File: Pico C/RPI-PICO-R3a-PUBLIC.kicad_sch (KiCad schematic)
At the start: 38 parts, among them IC1 W25Q16JVUXIQ, J3 USB_C_Receptacle_USB2.0_16P, J4 SM03B-SRSS-TB, Q1 DMG1012T-7, U2 RT6150B-33GQW, Y1 ECS-120-8-33-JGN-TR

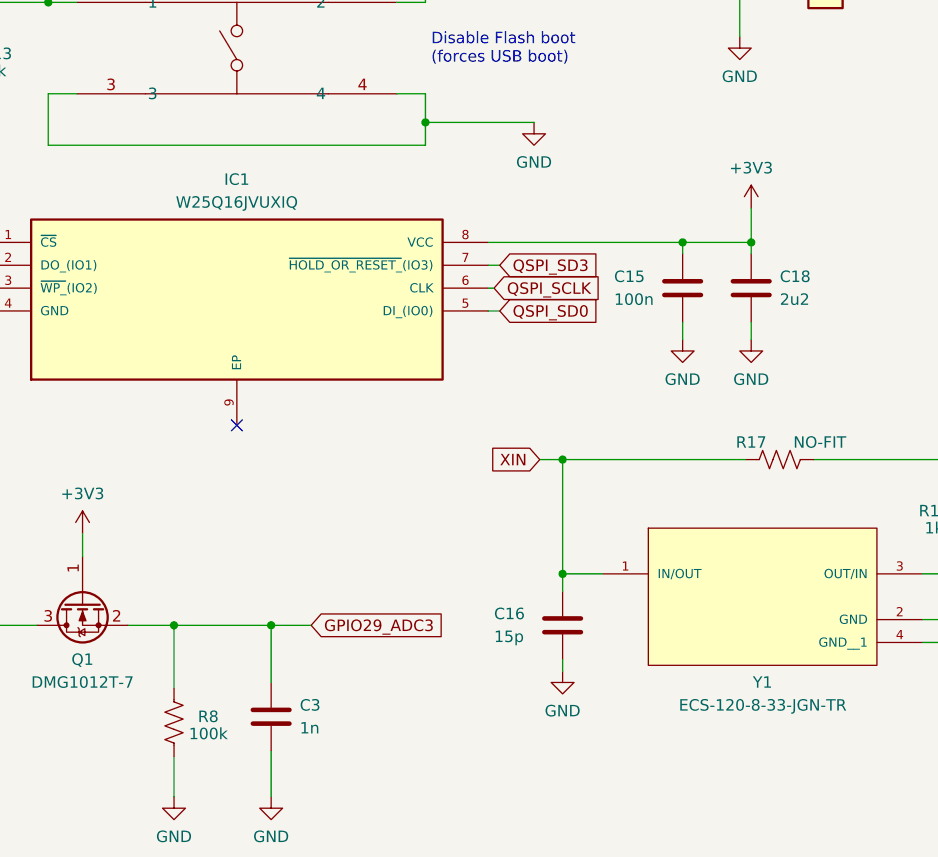
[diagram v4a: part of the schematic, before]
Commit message: Add files via upload
Updated component references to more closely match the original Pico.
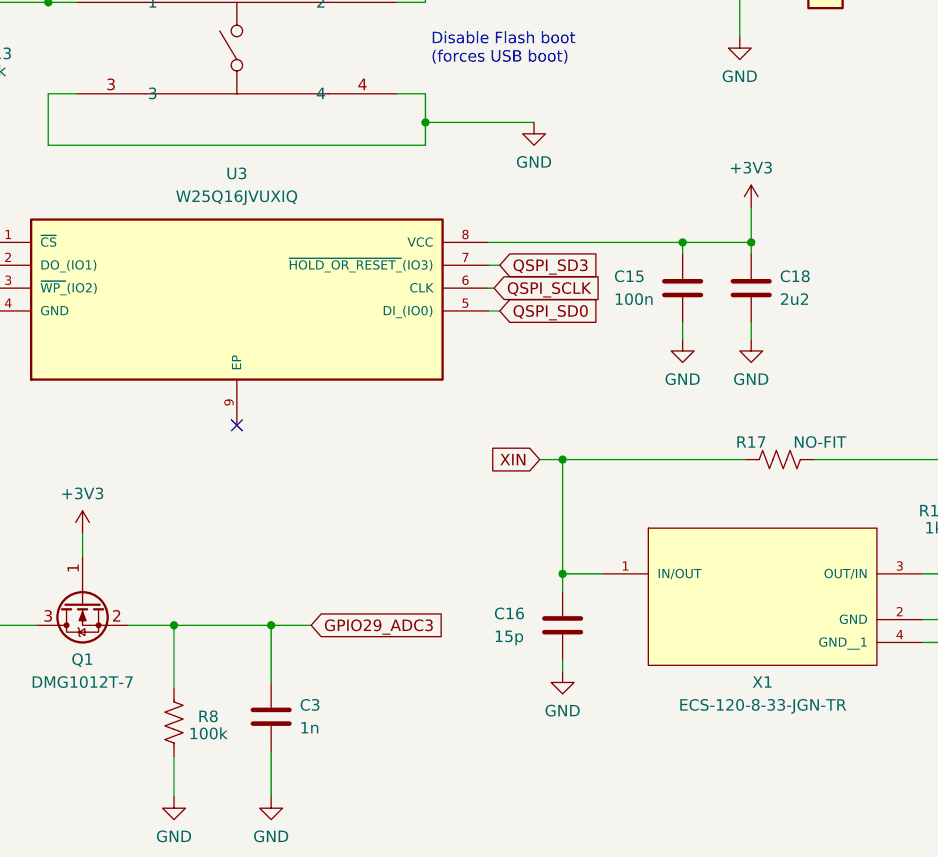
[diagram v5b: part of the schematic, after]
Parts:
- removed IC1: W25Q16JVUXIQ, Pico_C:SON50P300X200X60-9N, symbol Pico_C:W25Q16JVUXIQ
- removed Y1: ECS-120-8-33-JGN-TR, Pico_C:XTAL_ECS-120-8-33-JGN-TR, symbol Pico_C:ECS-120-8-33-JGN-TR
- added U3: W25Q16JVUXIQ, Pico_C:SON50P300X200X60-9N, symbol Pico_C:W25Q16JVUXIQ
- added X1: ECS-120-8-33-JGN-TR, ECS-120-8-33-JGN-TR:XTAL_ECS-120-8-33-JGN-TR, symbol Pico_C:ECS-120-8-33-JGN-TR
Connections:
- net +3V3: now also U3.8 (VCC)
- net GND: now also U3.4 (GND), X1.2 (GND), X1.4 (GND__1)
- net QSPI_SCLK: now also U3.6 (CLK)
- net QSPI_SD0: now also U3.5 (DI_(IO0))
- net QSPI_SD1: now also U3.2 (DO_(IO1))
- net QSPI_SD2: now also U3.3 (~{WP_}(IO2))
- net QSPI_SD3: now also U3.7 (~{HOLD_OR_RESET_}(IO3))
- net QSPI_SS: now also U3.1 (~{CS})
- net XIN: now also X1.1 (IN/OUT)
- net XR: now also X1.3 (OUT/IN)
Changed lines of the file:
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@@
 	)
 	(symbol
-		(lib_id "Pico_C:ECS-120-8-33-JGN-TR")
-		(at 207.645 149.225 0)
-		(unit 1)
-		(exclude_from_sim no)
-		(in_bom yes)
-		(on_board yes)
-		(dnp no)
-		(property "Reference" "Y1"
-			(at 207.645 158.75 0)
-			(effects
-				(font
-					(size 1.27 1.27)
-				)
-			)
-		)
-		(property "Value" "ECS-120-8-33-JGN-TR"
-			(at 207.645 161.29 0)
-			(effects
-				(font
-					(size 1.27 1.27)
-				)
-			)
-		)
-		(property "Footprint" "Pico_C:XTAL_ECS-120-8-33-JGN-TR"
-			(at 207.645 149.225 0)
-			(effects
-				(font
-					(size 1.27 1.27)
-				)
-				(justify bottom)
-				(hide yes)
-			)
-		)
-		(property "Datasheet" "https://ecsxtal.com/store/pdf/ecx-32.pdf"
-			(at 207.645 149.225 0)
-			(effects
-				(font
-					(size 1.27 1.27)
-				)
-				(hide yes)
-			)
-		)
-		(property "Description" ""
-			(at 207.645 149.225 0)
-			(effects
-				(font
-					(size 1.27 1.27)
-				)
-				(hide yes)
-			)
-		)
-		(pin "2"
-		)
-		(pin "3"
-		)
-		(pin "1"
-		)
-		(pin "4"
-		)
-		(instances
-			(project "RPI-PICO-R3a-PUBLIC"
-				(path "/f8a1033e-7d4e-4018-9b4c-1da5b150b31c"
-					(reference "Y1")
-					(unit 1)
-				)
-			)
-		)
-	)
-	(symbol
 		(lib_id "Device:R_US")
 		(at 77.47 50.165 180)
@@
 	)
 	(symbol
+		(lib_id "Pico_C:W25Q16JVUXIQ")
+		(at 121.285 109.855 0)
+		(unit 1)
+		(exclude_from_sim no)
+		(in_bom yes)
+		(on_board yes)
+		(dnp no)
+		(fields_autoplaced yes)
+		(property "Reference" "U3"
+			(at 149.225 102.235 0)
+			(effects
+				(font
+					(size 1.27 1.27)
+				)
+			)
+		)
+		(property "Value" "W25Q16JVUXIQ"
+			(at 149.225 104.775 0)
+			(effects
+				(font
+					(size 1.27 1.27)
+				)
+			)
+		)
+		(property "Footprint" "Pico_C:SON50P300X200X60-9N"
+			(at 121.285 109.855 0)
+			(effects
+				(font
+					(size 1.27 1.27)
+				)
+				(justify bottom)
+				(hide yes)
+			)
+		)
+		(property "Datasheet" "https://www.winbond.com/resource-files/w25q16jv%20spi%20revh%2004082019%20plus.pdf"
+			(at 121.285 109.855 0)
+			(effects
+				(font
+					(size 1.27 1.27)
+				)
+				(hide yes)
+			)
+		)
+		(property "Description" ""
+			(at 121.285 109.855 0)
+			(effects
+				(font
+					(size 1.27 1.27)
+				)
+				(hide yes)
+			)
+		)
+		(pin "9"
+		)
+		(pin "6"
+		)
+		(pin "3"
+		)
+		(pin "4"
+		)
+		(pin "1"
+		)
+		(pin "2"
+		)
+		(pin "5"
+		)
+		(pin "7"
+		)
+		(pin "8"
+		)
+		(instances
+			(project "RPI-PICO-R3a-PUBLIC"
+				(path "/f8a1033e-7d4e-4018-9b4c-1da5b150b31c"
+					(reference "U3")
+					(unit 1)
+				)
+			)
+		)
+	)
+	(symbol
 		(lib_id "Device:R_US")
 		(at 120.65 147.32 180)
@@
 	)
 	(symbol
+		(lib_id "Pico_C:ECS-120-8-33-JGN-TR")
+		(at 207.645 149.225 0)
+		(unit 1)
+		(exclude_from_sim no)
+		(in_bom yes)
+		(on_board yes)
+		(dnp no)
+		(property "Reference" "X1"
+			(at 207.645 158.75 0)
+			(effects
+				(font
+					(size 1.27 1.27)
+				)
+			)
+		)
+		(property "Value" "ECS-120-8-33-JGN-TR"
+			(at 207.645 161.29 0)
+			(effects
+				(font
+					(size 1.27 1.27)
+				)
+			)
+		)
+		(property "Footprint" "ECS-120-8-33-JGN-TR:XTAL_ECS-120-8-33-JGN-TR"
+			(at 207.645 149.225 0)
+			(effects
+				(font
+					(size 1.27 1.27)
+				)
+				(justify bottom)
+				(hide yes)
+			)
+		)
+		(property "Datasheet" "https://ecsxtal.com/store/pdf/ecx-32.pdf"
+			(at 207.645 149.225 0)
+			(effects
+				(font
+					(size 1.27 1.27)
+				)
+				(hide yes)
+			)
+		)
+		(property "Description" ""
+			(at 207.645 149.225 0)
+			(effects
+				(font
+					(size 1.27 1.27)
+				)
+				(hide yes)
+			)
+		)
+		(pin "4"
+		)
+		(pin "2"
+		)
+		(pin "1"
+		)
+		(pin "3"
+		)
+		(instances
+			(project "RPI-PICO-R3a-PUBLIC"
+				(path "/f8a1033e-7d4e-4018-9b4c-1da5b150b31c"
+					(reference "X1")
+					(unit 1)
+				)
+			)
+		)
+	)
+	(symbol
 		(lib_id "Pico_C:SM03B-SRSS-TB_LF__SN_")
 		(at 269.875 135.89 0)
@@
 					(unit 1)
 				)
-			)
-		)
-	)
-	(symbol
-		(lib_id "Pico_C:W25Q16JVUXIQ")
-		(at 121.285 109.855 0)
-		(unit 1)
-		(exclude_from_sim no)
-		(in_bom yes)
-		(on_board yes)
-		(dnp no)
-		(fields_autoplaced yes)
-		(property "Reference" "IC1"
-			(at 149.225 102.87 0)
-			(effects
-				(font
-					(size 1.27 1.27)
-				)
-			)
-		)
-		(property "Value" "W25Q16JVUXIQ"
-			(at 149.225 105.41 0)
-			(effects
-				(font
-					(size 1.27 1.27)
-				)
-			)
-		)
-		(property "Footprint" "Pico_C:SON50P300X200X60-9N"
-			(at 121.285 109.855 0)
-			(effects
-				(font
-					(size 1.27 1.27)
-				)
-				(justify bottom)
-				(hide yes)
-			)
-		)
-		(property "Datasheet" "https://www.winbond.com/resource-files/w25q16jv%20spi%20revh%2004082019%20plus.pdf"
-			(at 121.285 109.855 0)
-			(effects
-				(font
-					(size 1.27 1.27)
-				)
-				(hide yes)
-			)
-		)
-		(property "Description" ""
-			(at 121.285 109.855 0)
-			(effects
-				(font
-					(size 1.27 1.27)
-				)
-				(hide yes)
-			)
-		)
-		(pin "9"
-		)
-		(pin "8"
-		)
-		(pin "4"
-		)
-		(pin "7"
-		)
-		(pin "2"
-		)
-		(pin "6"
-		)
-		(pin "1"
-		)
-		(pin "3"
-		)
-		(pin "5"
-		)
-		(instances
-			(project "RPI-PICO-R3a-PUBLIC"
-				(path "/f8a1033e-7d4e-4018-9b4c-1da5b150b31c"
-					(reference "IC1")
-					(unit 1)
-				)

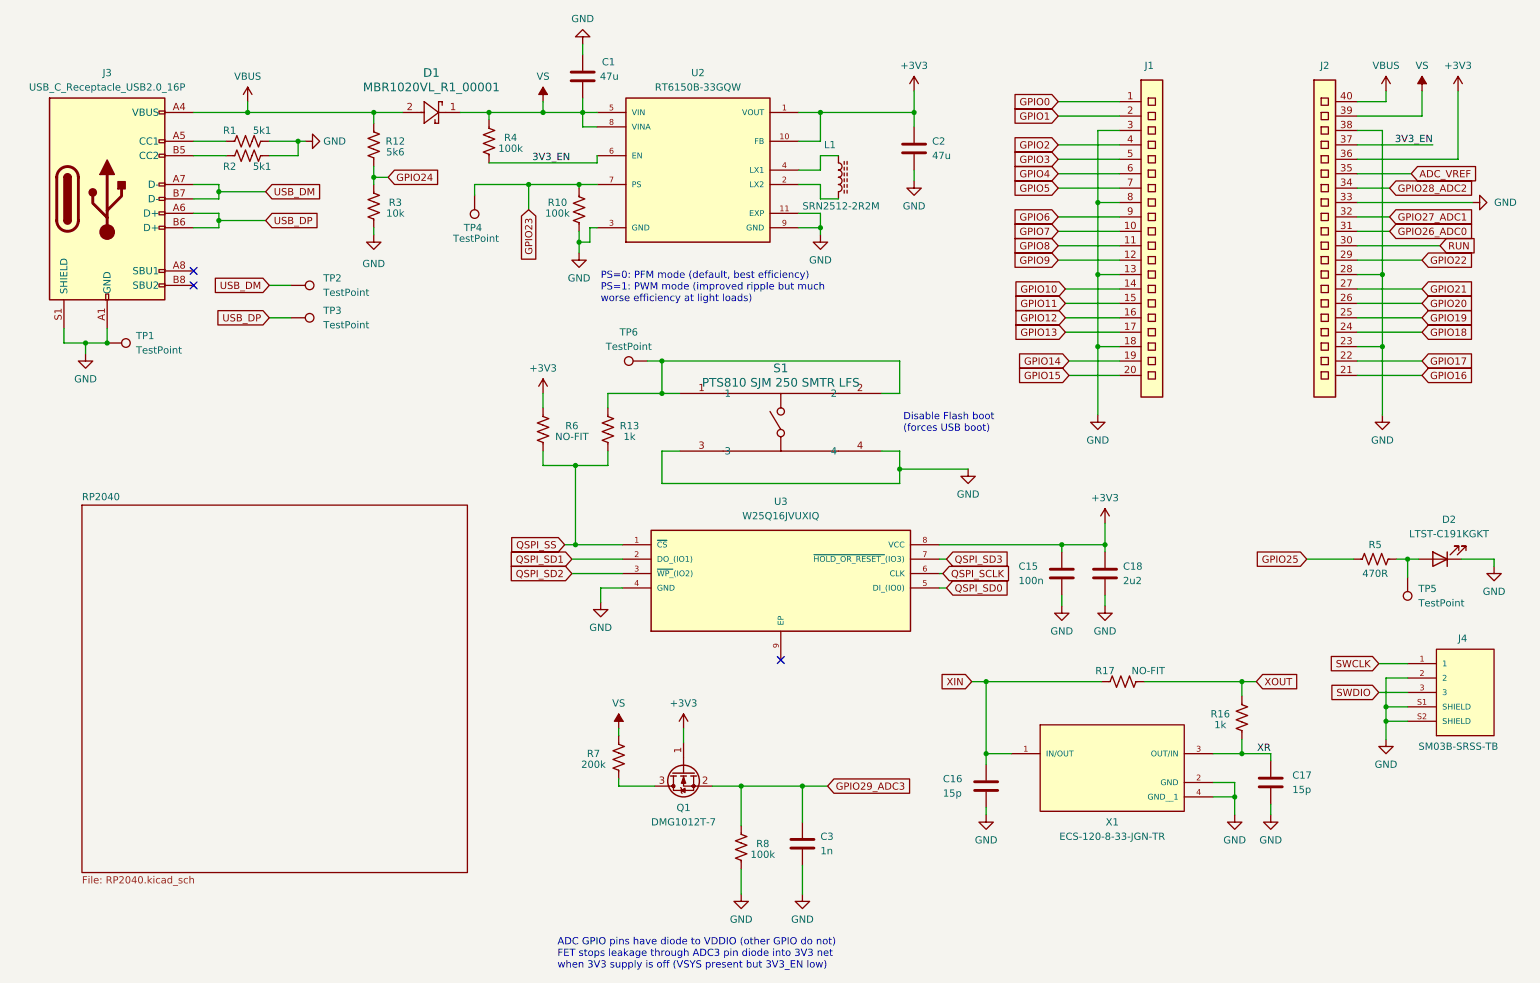
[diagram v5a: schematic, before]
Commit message: Add files via upload
Changed resistor reference numbers to match the real Pico H.
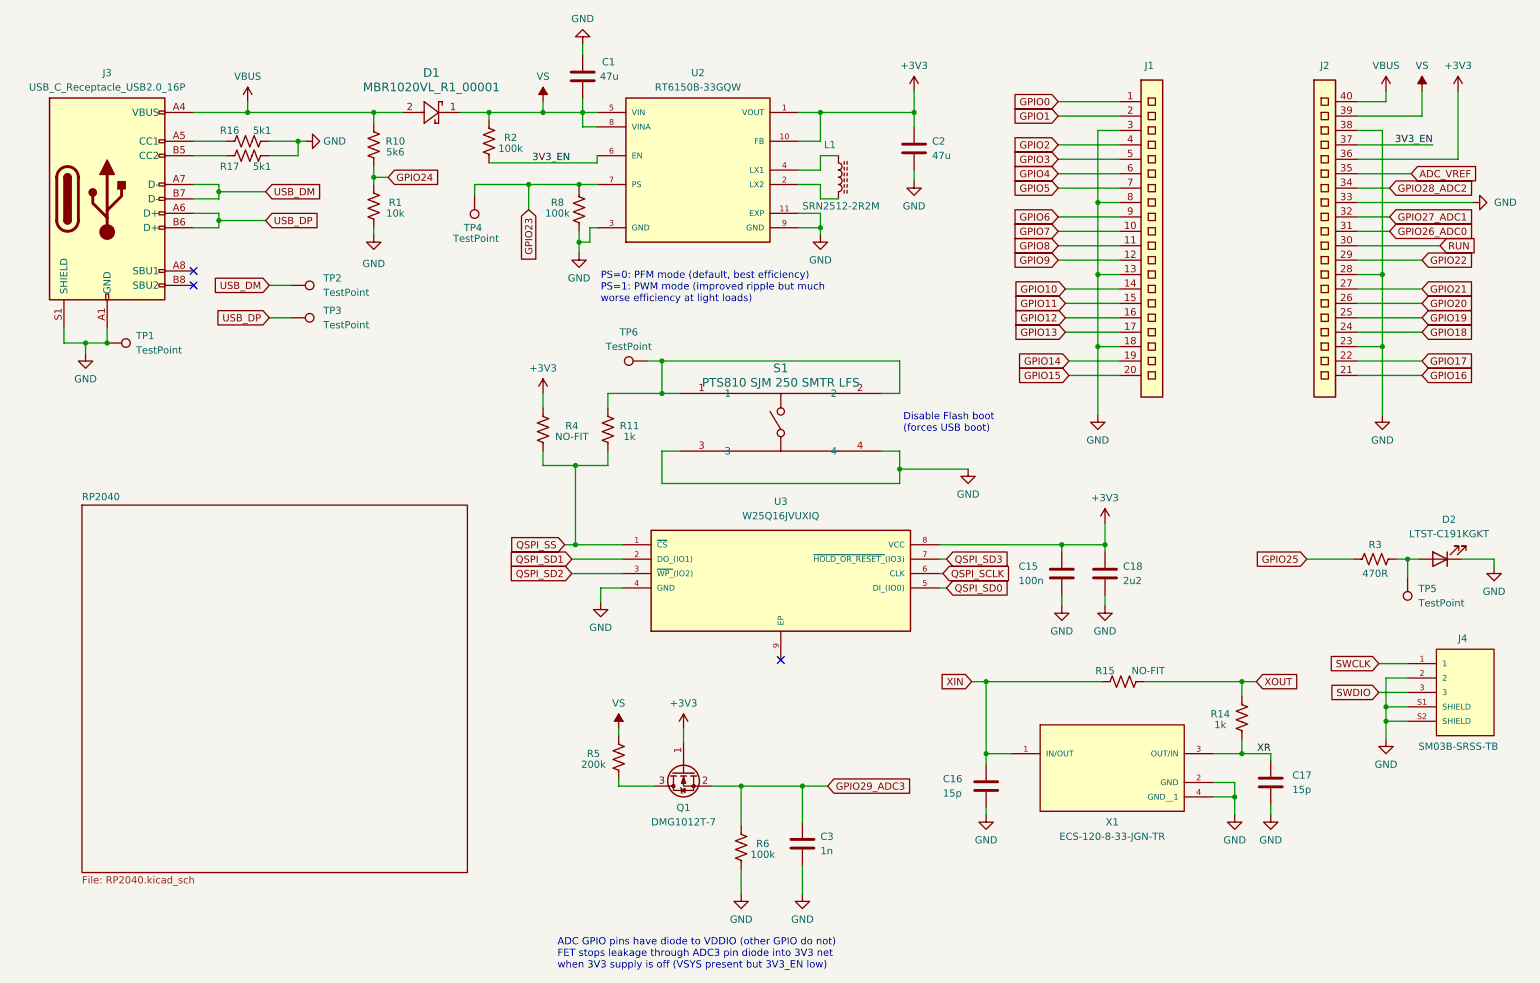
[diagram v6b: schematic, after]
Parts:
- renumbered R3 to R1, R12 to R10, R13 to R11, R16 to R14, R17 to R15, R1 to R16, R2 to R17, R4 to R2, R5 to R3, R6 to R4, R7 to R5, R8 to R6, R10 to R8
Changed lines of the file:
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@@
 		(on_board yes)
 		(dnp no)
-		(property "Reference" "R4"
+		(property "Reference" "R2"
 			(at 101.6 38.1 0)
 			(effects
@@
 			(project "RPI-PICO-R3a-PUBLIC"
 				(path "/f8a1033e-7d4e-4018-9b4c-1da5b150b31c"
-					(reference "R4")
+					(reference "R2")
 					(unit 1)
 				)
@@
 		(on_board yes)
 		(dnp no)
-		(property "Reference" "R16"
+		(property "Reference" "R14"
 			(at 226.695 139.7 0)
 			(effects
@@
 			(project "RPI-PICO-R3a-PUBLIC"
 				(path "/f8a1033e-7d4e-4018-9b4c-1da5b150b31c"
-					(reference "R16")
+					(reference "R14")
 					(unit 1)
 				)
@@
 		(on_board yes)
 		(dnp no)
-		(property "Reference" "R3"
+		(property "Reference" "R1"
 			(at 81.28 49.53 0)
 			(effects
@@
 			(project "RPI-PICO-R3a-PUBLIC"
 				(path "/f8a1033e-7d4e-4018-9b4c-1da5b150b31c"
-					(reference "R3")
+					(reference "R1")
 					(unit 1)
 				)
@@
 		(on_board yes)
 		(dnp no)
-		(property "Reference" "R1"
+		(property "Reference" "R16"
 			(at 52.07 36.83 90)
 			(effects
@@
 			(project "RPI-PICO-R3a-PUBLIC"
 				(path "/f8a1033e-7d4e-4018-9b4c-1da5b150b31c"
-					(reference "R1")
+					(reference "R16")
 					(unit 1)
 				)
@@
 		(on_board yes)
 		(dnp no)
-		(property "Reference" "R6"
+		(property "Reference" "R4"
 			(at 112.395 88.9 0)
 			(effects
@@
 			(project "RPI-PICO-R3a-PUBLIC"
 				(path "/f8a1033e-7d4e-4018-9b4c-1da5b150b31c"
-					(reference "R6")
+					(reference "R4")
 					(unit 1)
 				)
@@
 		(on_board yes)
 		(dnp no)
-		(property "Reference" "R13"
+		(property "Reference" "R11"
 			(at 122.555 88.9 0)
 			(effects
@@
 			(project "RPI-PICO-R3a-PUBLIC"
 				(path "/f8a1033e-7d4e-4018-9b4c-1da5b150b31c"
-					(reference "R13")
+					(reference "R11")
 					(unit 1)
 				)
@@
 		(on_board yes)
 		(dnp no)
-		(property "Reference" "R7"
+		(property "Reference" "R5"
 			(at 116.205 146.685 0)
 			(effects
@@
 			(project "RPI-PICO-R3a-PUBLIC"
 				(path "/f8a1033e-7d4e-4018-9b4c-1da5b150b31c"
-					(reference "R7")
+					(reference "R5")
 					(unit 1)
 				)
@@
 		(on_board yes)
 		(dnp no)
-		(property "Reference" "R10"
+		(property "Reference" "R8"
 			(at 109.855 49.53 0)
 			(effects
@@
 			(project "RPI-PICO-R3a-PUBLIC"
 				(path "/f8a1033e-7d4e-4018-9b4c-1da5b150b31c"
-					(reference "R10")
+					(reference "R8")
 					(unit 1)
 				)
@@
 		(on_board yes)
 		(dnp no)
-		(property "Reference" "R17"
+		(property "Reference" "R15"
 			(at 206.375 132.08 90)
 			(effects
@@
 			(project "RPI-PICO-R3a-PUBLIC"
 				(path "/f8a1033e-7d4e-4018-9b4c-1da5b150b31c"
-					(reference "R17")
+					(reference "R15")
 					(unit 1)
 				)
@@
 		(on_board yes)
 		(dnp no)
-		(property "Reference" "R5"
+		(property "Reference" "R3"
 			(at 254 109.855 90)
 			(effects
@@
 			(project "RPI-PICO-R3a-PUBLIC"
 				(path "/f8a1033e-7d4e-4018-9b4c-1da5b150b31c"
-					(reference "R5")
+					(reference "R3")
 					(unit 1)
 				)
@@
 		(on_board yes)
 		(dnp no)
-		(property "Reference" "R8"
+		(property "Reference" "R6"
 			(at 146.05 162.56 0)
 			(effects
@@
 			(project "RPI-PICO-R3a-PUBLIC"
 				(path "/f8a1033e-7d4e-4018-9b4c-1da5b150b31c"
-					(reference "R8")
+					(reference "R6")
 					(unit 1)
 				)
@@
 		(on_board yes)
 		(dnp no)
-		(property "Reference" "R12"
+		(property "Reference" "R10"
 			(at 81.28 38.735 0)
 			(effects
@@
 			(project "RPI-PICO-R3a-PUBLIC"
 				(path "/f8a1033e-7d4e-4018-9b4c-1da5b150b31c"
-					(reference "R12")
+					(reference "R10")
 					(unit 1)
 				)
@@
 		(on_board yes)
 		(dnp no)
-		(property "Reference" "R2"
+		(property "Reference" "R17"
 			(at 52.07 43.18 90)
 			(effects
@@
 			(project "RPI-PICO-R3a-PUBLIC"
 				(path "/f8a1033e-7d4e-4018-9b4c-1da5b150b31c"
-					(reference "R2")
+					(reference "R17")
 					(unit 1)
 				)

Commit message: Add files via upload
Updated X1's footprint for schematic parity in DRC.
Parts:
- X1: footprint ECS-120-8-33-JGN-TR:XTAL_ECS-120-8-33-JGN-TR -> Pico_C:XTAL_ECS-120-8-33-JGN-TR
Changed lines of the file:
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@@
 			)
 		)
-		(property "Footprint" "ECS-120-8-33-JGN-TR:XTAL_ECS-120-8-33-JGN-TR"
+		(property "Footprint" "Pico_C:XTAL_ECS-120-8-33-JGN-TR"
 			(at 207.645 149.225 0)
 			(effects
